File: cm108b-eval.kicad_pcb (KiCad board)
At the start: 2 copper layers, 60 x 50 mm, 44 parts, among them IC1 CM108B, J1 SPKR, J2 MIC, J3 RADIO_DATA, SW1 MUTE_REC, SW2 MUTE_PLAY, SW3 VOL_DN, SW4 VOL_UP

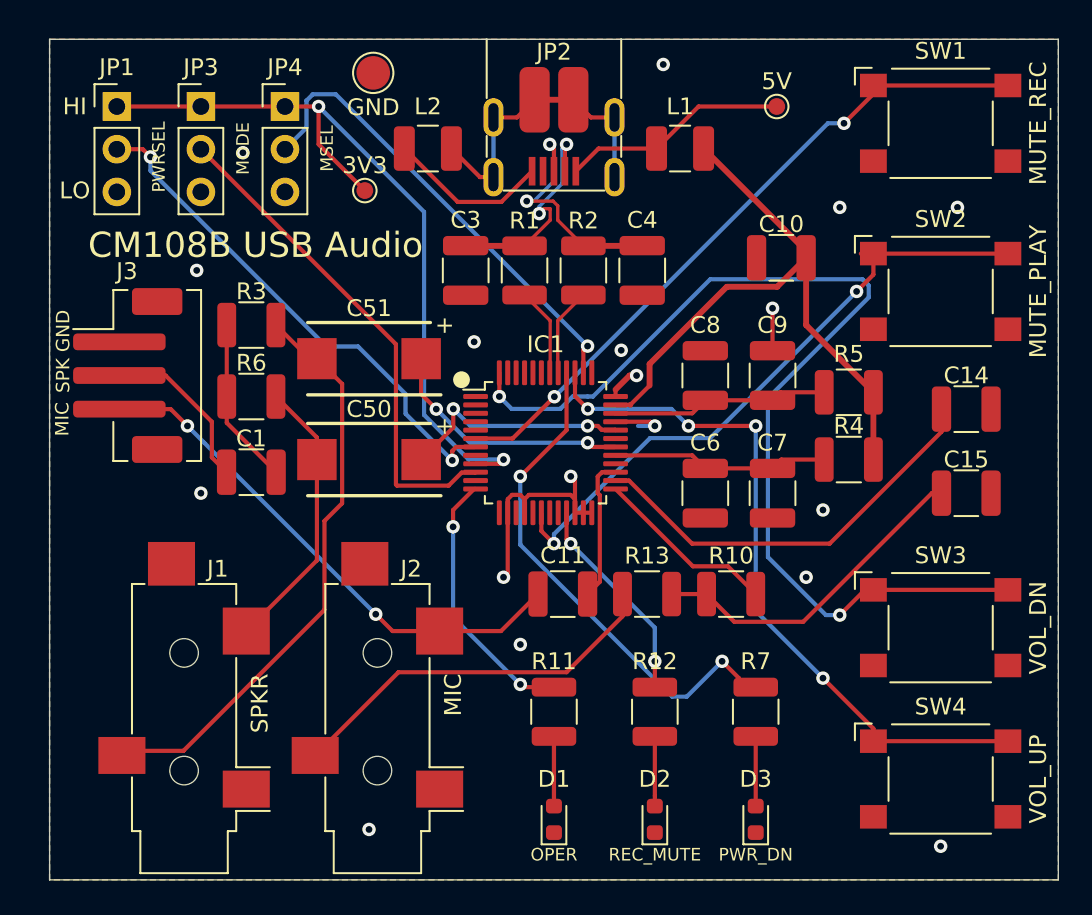
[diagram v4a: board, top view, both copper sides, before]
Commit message: Copy from HS100B project to get identical layouts
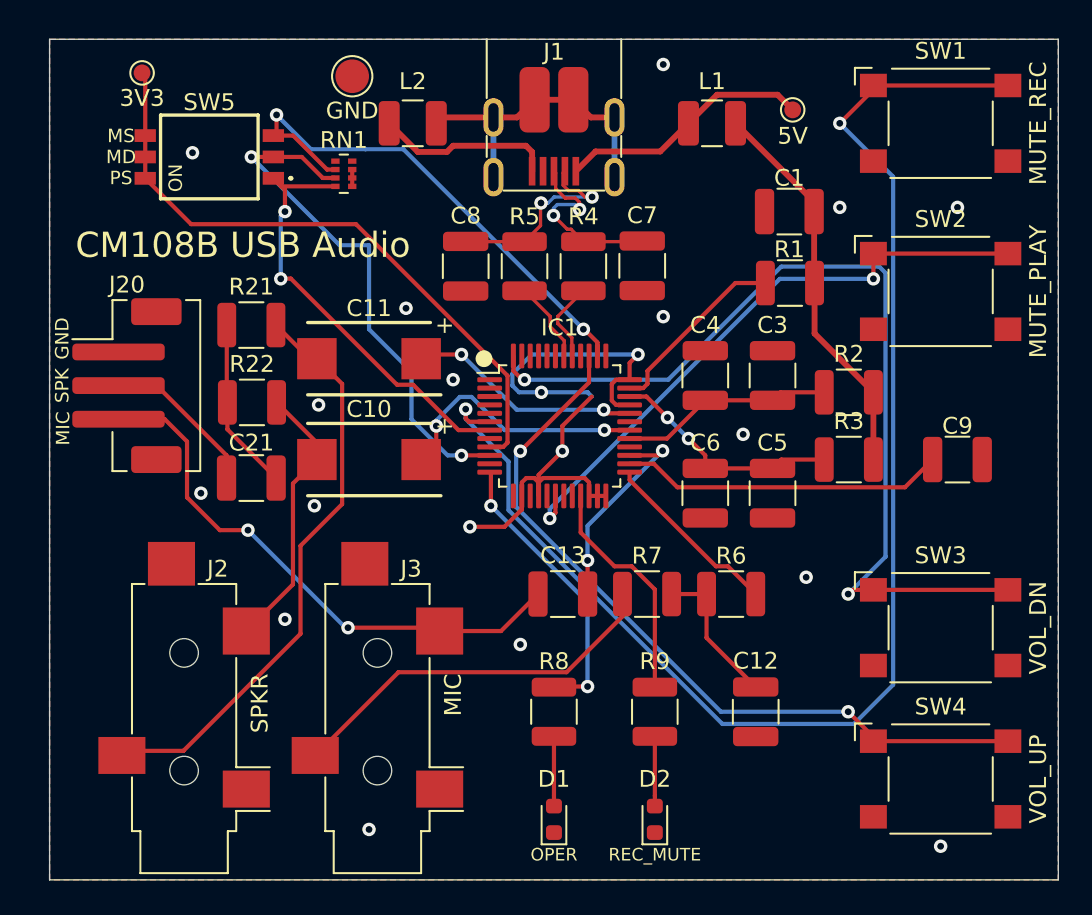
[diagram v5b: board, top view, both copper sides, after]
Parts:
- removed D3: PWR_DN, LED_SMD:LED_0603_1608Metric
- removed JP1: PWRSEL, Connector_PinHeader_2.54mm:PinHeader_1x03_P2.54mm_Vertical
- removed JP2: USB_MICRO_B, CUI:UJ2-MIBH-4-SMT
- removed JP3: MODE, Connector_PinHeader_2.54mm:PinHeader_1x03_P2.54mm_Vertical
- removed JP4: MSEL, Connector_PinHeader_2.54mm:PinHeader_1x03_P2.54mm_Vertical
- removed the R7 at (172.0, 110.0)
- added J1: USB_B_Micro, CUI:UJ2-MIBH-4-SMT, F.Cu at (160.0, 70.0)
- added R1: 0Ω, Resistor_SMD:R_1210_3225Metric, F.Cu at (174.0, 84.5)
- added RN1: 10KΩ, Resistor_SMD:R_Array_Concave_4x0402, F.Cu at (147.5, 78.0)
- added SW5: SW_DIP_x03, Wurth:416131160803, F.Cu at (139.5, 77.0)
- L1, L2: value L -> Ferrite_Bead
- moved C12 18.1 mm to (172.0, 110.0), turned to 90 degrees
- moved TP3 15.0 mm to (135.5, 72.0)
- moved C9 3.05 mm to (184.0, 95.0)
- moved C1 2.79 mm to (174.0, 80.2)
- moved L1 2.42 mm to (169.4, 75.0)
- moved L2 1.75 mm to (151.6, 75.0)
- moved IC1 1.30 mm to (160.3, 93.0)
- moved TP1 1.27 mm to (148.0, 72.2)
- moved TP2 0.97 mm to (174.2, 74.2)
- moved J20 0.60 mm to (134.6, 90.6)
- moved R22 0.35 mm to (142.0, 91.6)
- moved C21 0.35 mm to (142.0, 96.1)
- moved C7 0.28 mm to (165.2, 83.5)
- moved C8 0.25 mm to (154.8, 83.5)
- moved R4 0.25 mm to (161.8, 83.5)
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- renumbered C10 to C1, C50 to C10, C51 to C11, C15 to C12, C11 to C13, C1 to C21, C9 to C3, C8 to C4, C7 to C5, C4 to C7, C3 to C8, C14 to C9, J1 to J2, J3 to J20, J2 to J3, R5 to R2, R3 to R21, R6 to R22, R4 to R3, R2 to R4, R1 to R5, R10 to R6, R13 to R7, R11 to R8, R12 to R9
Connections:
- C10 pad 1: Net-(C50-Pad1) -> Net-(C10-Pad1)
- C11 pad 1: Net-(C51-Pad1) -> Net-(C11-Pad1)
- C3 pad 1: Net-(C8-Pad1) -> /AVDD1
- C4 pad 1: Net-(C8-Pad1) -> /AVDD1
- C5 pad 1: Net-(C6-Pad1) -> /AVDD2
- C6 pad 1: Net-(C6-Pad1) -> /AVDD2
- IC1 pad 29: Net-(C6-Pad1) -> /AVDD1
- IC1 pad 30: Net-(C51-Pad1) -> Net-(C10-Pad1)
- IC1 pad 32: Net-(C50-Pad1) -> Net-(C11-Pad1)
- IC1 pad 34: Net-(C8-Pad1) -> /AVDD2
- IC1 pad 35: VBUS -> /DVDD
- IC1 pad 40: /PDSW -> (no net)
- R2 pad 1: Net-(C8-Pad1) -> /AVDD1
- R3 pad 1: Net-(C6-Pad1) -> /AVDD2
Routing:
- net /MUTER: track 40.7 -> 84.0 mm
- net /PDSW: track 29.9 -> 0.00 mm, vias 2 -> 0
- net GND: track 31.7 -> 50.2 mm, vias 18 -> 20
- net Net-(C10-Pad1): track 0.00 -> 15.6 mm, vias 0 -> 2
- net VBUS: track 38.4 -> 23.4 mm
- net Net-(C51-Pad1): track 15.0 -> 0.00 mm, vias 2 -> 0
- net /AVDD2: track 0.00 -> 14.0 mm, vias 0 -> 2
- net Net-(C50-Pad1): track 14.0 -> 0.00 mm, vias 2 -> 0
- net Net-(C11-Pad1): track 0.00 -> 14.0 mm, vias 0 -> 2
- net Net-(C6-Pad1): track 13.0 -> 0.00 mm
- net Net-(C8-Pad1): track 12.9 -> 0.00 mm
- net /AVDD1: track 0.00 -> 12.7 mm
- net /DVDD: track 0.00 -> 11.1 mm
- net Net-(C12-Pad2): track 19.9 -> 8.81 mm
- net +3V3: track 46.7 -> 37.9 mm, vias 2 -> 0
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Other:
- net class Signal added: clearance 0.2, trace_width 0.2, via_dia 0.8, via_drill 0.4
- board text added: "CM108B Audio Evaluation Board v6 C. Keller 2021-04-21 https://github.com/k0swe/cm108b-eval"
- board text removed: "CM108B Audio Evaluation Board v5 C. Keller 2021-04-21 https://github.com/k0swe/cm108b-eval"
- board text removed: "HI"
- board text removed: "LO"

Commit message: Add OSHW logo
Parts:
- added LOGO1: Logo_Open_Hardware_Small, Symbol:OSHW-Logo2_9.8x8mm_SilkScreen, B.Cu at (170.0, 100.0)
